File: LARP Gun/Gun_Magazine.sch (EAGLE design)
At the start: 1 part

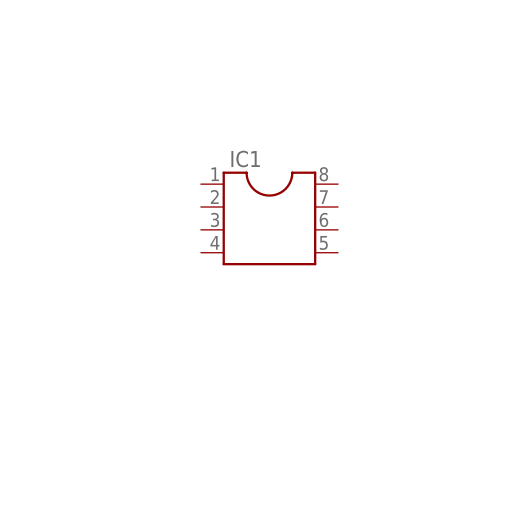
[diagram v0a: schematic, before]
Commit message: Added pull down resistors to the magazine board.
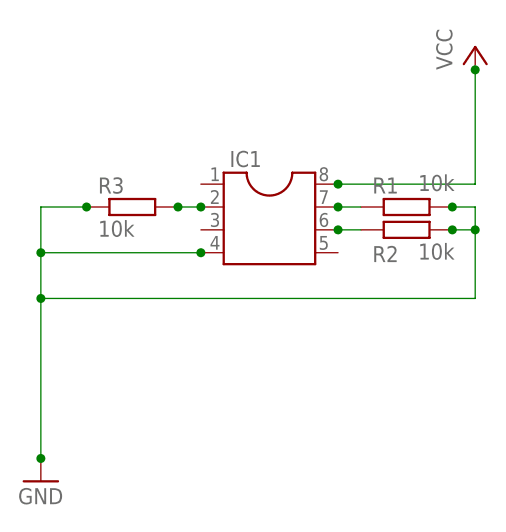
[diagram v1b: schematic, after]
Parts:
- added R1, R2, R3: 10k, resistor:R-EU_0207/7
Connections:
- new net GND: IC1.4, R1.2, R2.2, R3.1
- new net N$10: IC1.7, R1.1
- new net N$11: IC1.6, R2.1
- new net N$9: IC1.2, R3.2
- new net VCC: IC1.8
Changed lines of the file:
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@@
 <layer number="97" name="Info" color="7" fill="1" visible="yes" active="yes"/>
 <layer number="98" name="Guide" color="6" fill="1" visible="yes" active="yes"/>
+<layer number="99" name="SpiceOrder" color="5" fill="1" visible="yes" active="yes"/>
 <layer number="100" name="Otwor_montazowy" color="6" fill="1" visible="yes" active="yes"/>
 <layer number="101" name="DOC" color="7" fill="1" visible="yes" active="yes"/>
@@
 <part name="FRAME1" library="frames" deviceset="A4L-LOC" device=""/>
 <part name="IC1" library="ic-package" deviceset="DIL8" device=""/>
+<part name="R1" library="resistor" deviceset="R-EU_" device="0207/7" value="10k"/>
+<part name="R2" library="resistor" deviceset="R-EU_" device="0207/7" value="10k"/>
+<part name="R3" library="resistor" deviceset="R-EU_" device="0207/7" value="10k"/>
+<part name="GND1" library="supply1" deviceset="GND" device=""/>
+<part name="P+1" library="supply1" deviceset="VCC" device=""/>
 </parts>
 <sheets>
@@
 <instance part="FRAME1" gate="G$1" x="0" y="0"/>
 <instance part="IC1" gate="G$1" x="152.4" y="104.14"/>
+<instance part="R1" gate="G$1" x="167.64" y="104.14" smashed="yes">
+<attribute name="NAME" x="163.83" y="105.6386" size="1.778" layer="95"/>
+<attribute name="VALUE" x="168.91" y="105.918" size="1.778" layer="96"/>
+</instance>
+<instance part="R2" gate="G$1" x="167.64" y="101.6" smashed="yes">
+<attribute name="NAME" x="163.83" y="98.0186" size="1.778" layer="95"/>
+<attribute name="VALUE" x="168.91" y="98.298" size="1.778" layer="96"/>
+</instance>
+<instance part="R3" gate="G$1" x="137.16" y="104.14"/>
+<instance part="GND1" gate="1" x="127" y="73.66"/>
+<instance part="P+1" gate="VCC" x="175.26" y="121.92"/>
 </instances>
 <busses>
 </busses>
 <nets>
+<net name="VCC" class="0">
+<segment>
+<pinref part="IC1" gate="G$1" pin="8"/>
+<pinref part="P+1" gate="VCC" pin="VCC"/>
+<wire x1="160.02" y1="106.68" x2="175.26" y2="106.68" width="0.1524" layer="91"/>
+<wire x1="175.26" y1="106.68" x2="175.26" y2="119.38" width="0.1524" layer="91"/>
+<junction x="160.02" y="106.68"/>
+<junction x="175.26" y="119.38"/>
+</segment>
+</net>
+<net name="GND" class="0">
+<segment>
+<pinref part="IC1" gate="G$1" pin="4"/>
+<pinref part="GND1" gate="1" pin="GND"/>
+<wire x1="144.78" y1="99.06" x2="127" y2="99.06" width="0.1524" layer="91"/>
+<wire x1="127" y1="99.06" x2="127" y2="93.98" width="0.1524" layer="91"/>
+<pinref part="R3" gate="G$1" pin="1"/>
+<wire x1="127" y1="93.98" x2="127" y2="76.2" width="0.1524" layer="91"/>
+<wire x1="132.08" y1="104.14" x2="127" y2="104.14" width="0.1524" layer="91"/>
+<wire x1="127" y1="104.14" x2="127" y2="99.06" width="0.1524" layer="91"/>
+<pinref part="R1" gate="G$1" pin="2"/>
+<wire x1="172.72" y1="104.14" x2="175.26" y2="104.14" width="0.1524" layer="91"/>
+<wire x1="175.26" y1="104.14" x2="175.26" y2="101.6" width="0.1524" layer="91"/>
+<wire x1="175.26" y1="101.6" x2="175.26" y2="93.98" width="0.1524" layer="91"/>
+<wire x1="175.26" y1="93.98" x2="127" y2="93.98" width="0.1524" layer="91"/>
+<pinref part="R2" gate="G$1" pin="2"/>
+<wire x1="172.72" y1="101.6" x2="175.26" y2="101.6" width="0.1524" layer="91"/>
+<junction x="172.72" y="104.14"/>
+<junction x="172.72" y="101.6"/>
+<junction x="132.08" y="104.14"/>
+<junction x="127" y="99.06"/>
+<junction x="127" y="93.98"/>
+<junction x="144.78" y="99.06"/>
+<junction x="175.26" y="101.6"/>
+<junction x="127" y="76.2"/>
+</segment>
+</net>
+<net name="N$9" class="0">
+<segment>
+<pinref part="IC1" gate="G$1" pin="2"/>
+<pinref part="R3" gate="G$1" pin="2"/>
+<wire x1="144.78" y1="104.14" x2="142.24" y2="104.14" width="0.1524" layer="91"/>
+<junction x="144.78" y="104.14"/>
+<junction x="142.24" y="104.14"/>
+</segment>
+</net>
+<net name="N$10" class="0">
+<segment>
+<pinref part="IC1" gate="G$1" pin="7"/>
+<pinref part="R1" gate="G$1" pin="1"/>
+<wire x1="160.02" y1="104.14" x2="162.56" y2="104.14" width="0.1524" layer="91"/>
+<junction x="160.02" y="104.14"/>
+</segment>
+</net>
+<net name="N$11" class="0">
+<segment>
+<pinref part="IC1" gate="G$1" pin="6"/>
+<pinref part="R2" gate="G$1" pin="1"/>
+<wire x1="160.02" y1="101.6" x2="162.56" y2="101.6" width="0.1524" layer="91"/>
+<junction x="160.02" y="101.6"/>
+</segment>
+</net>
 </nets>
 </sheet>
